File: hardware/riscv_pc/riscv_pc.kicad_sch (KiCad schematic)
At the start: 12 parts, among them J1 te_m.2_b, J2 te_m.2_b, J3 Conn_01x06, J4 HDMI_A, J5 AudioJack3, SW1 TS-1187A-C-D-B

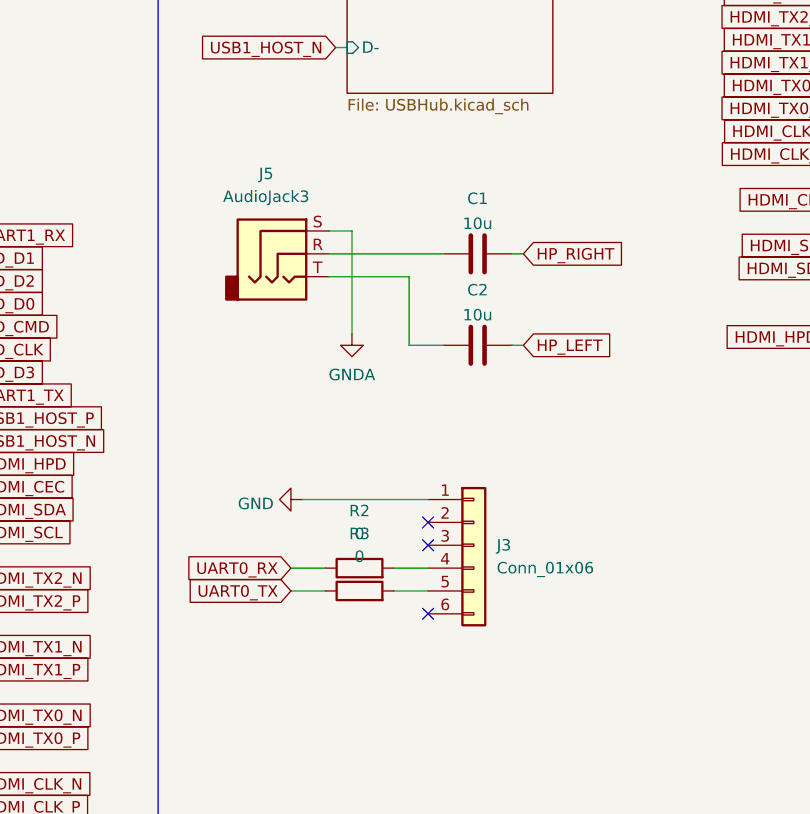
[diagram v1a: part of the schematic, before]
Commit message: Add ESD protection to AUX port
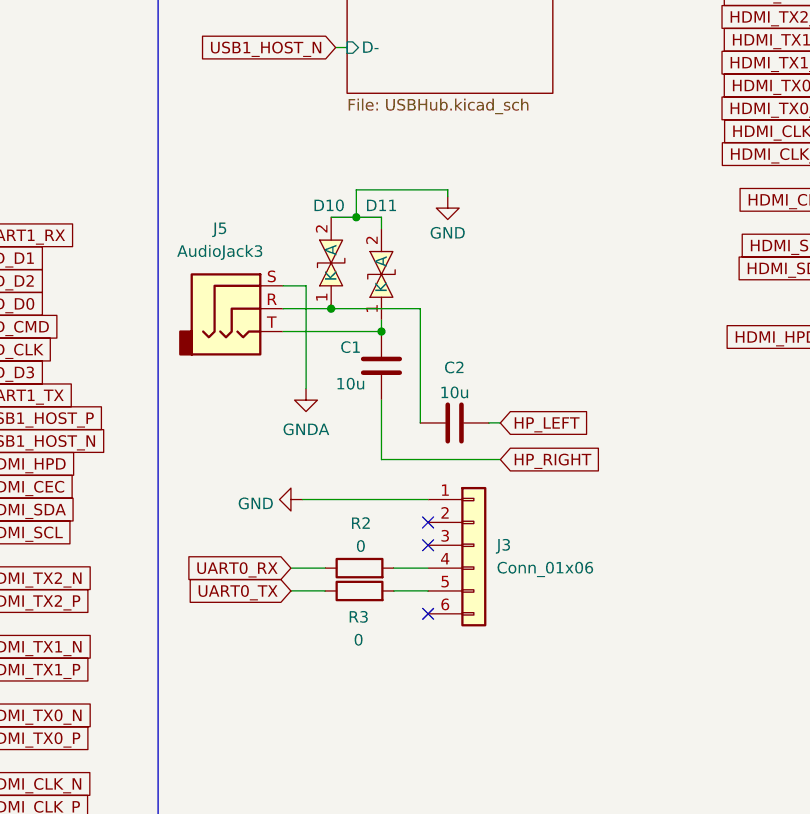
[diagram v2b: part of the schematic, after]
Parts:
- added D10, D11: GBLC08C-LF-T7, easyeda2kicad:SOD-323_L1.8-W1.3-LS2.5-BI, symbol lcsc:GBLC08C-LF-T7
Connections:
- net GND: now also D10.2 (A), D11.2 (A)
- net at C1.1: now also J5.T, D11.1 (K); no longer J5.R
- net at C2.1: now also J5.R, D10.1 (K); no longer J5.T
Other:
- moved on the sheet: C1, C2, J5

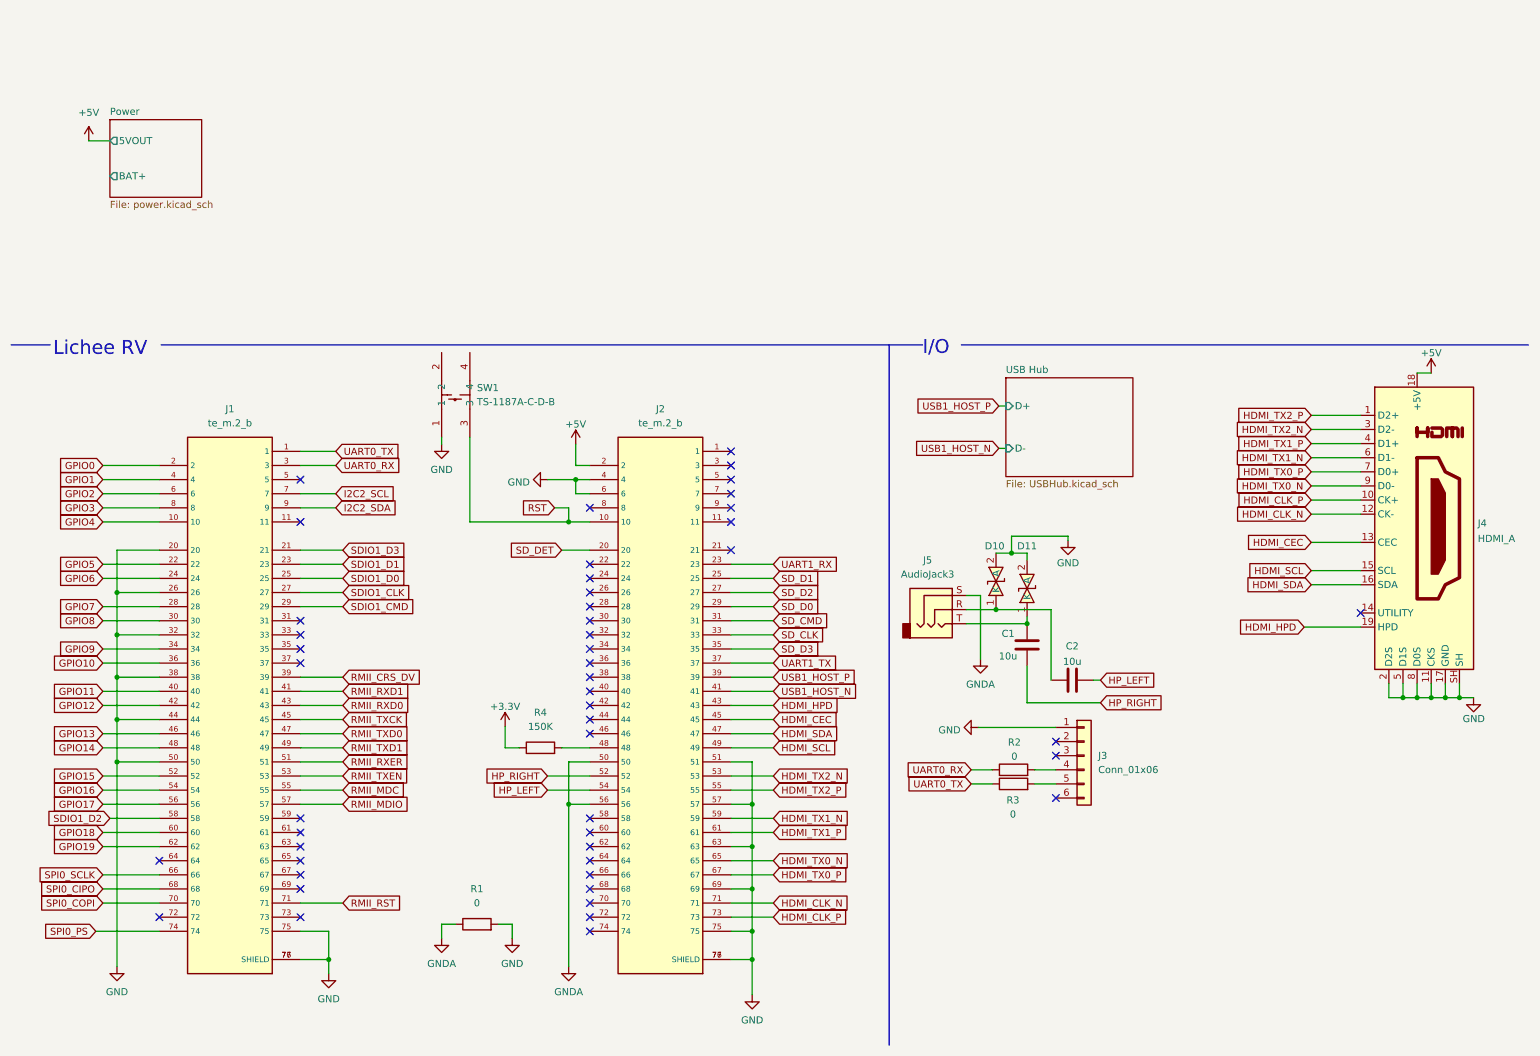
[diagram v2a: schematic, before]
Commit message: Add ESD protection to HDMI
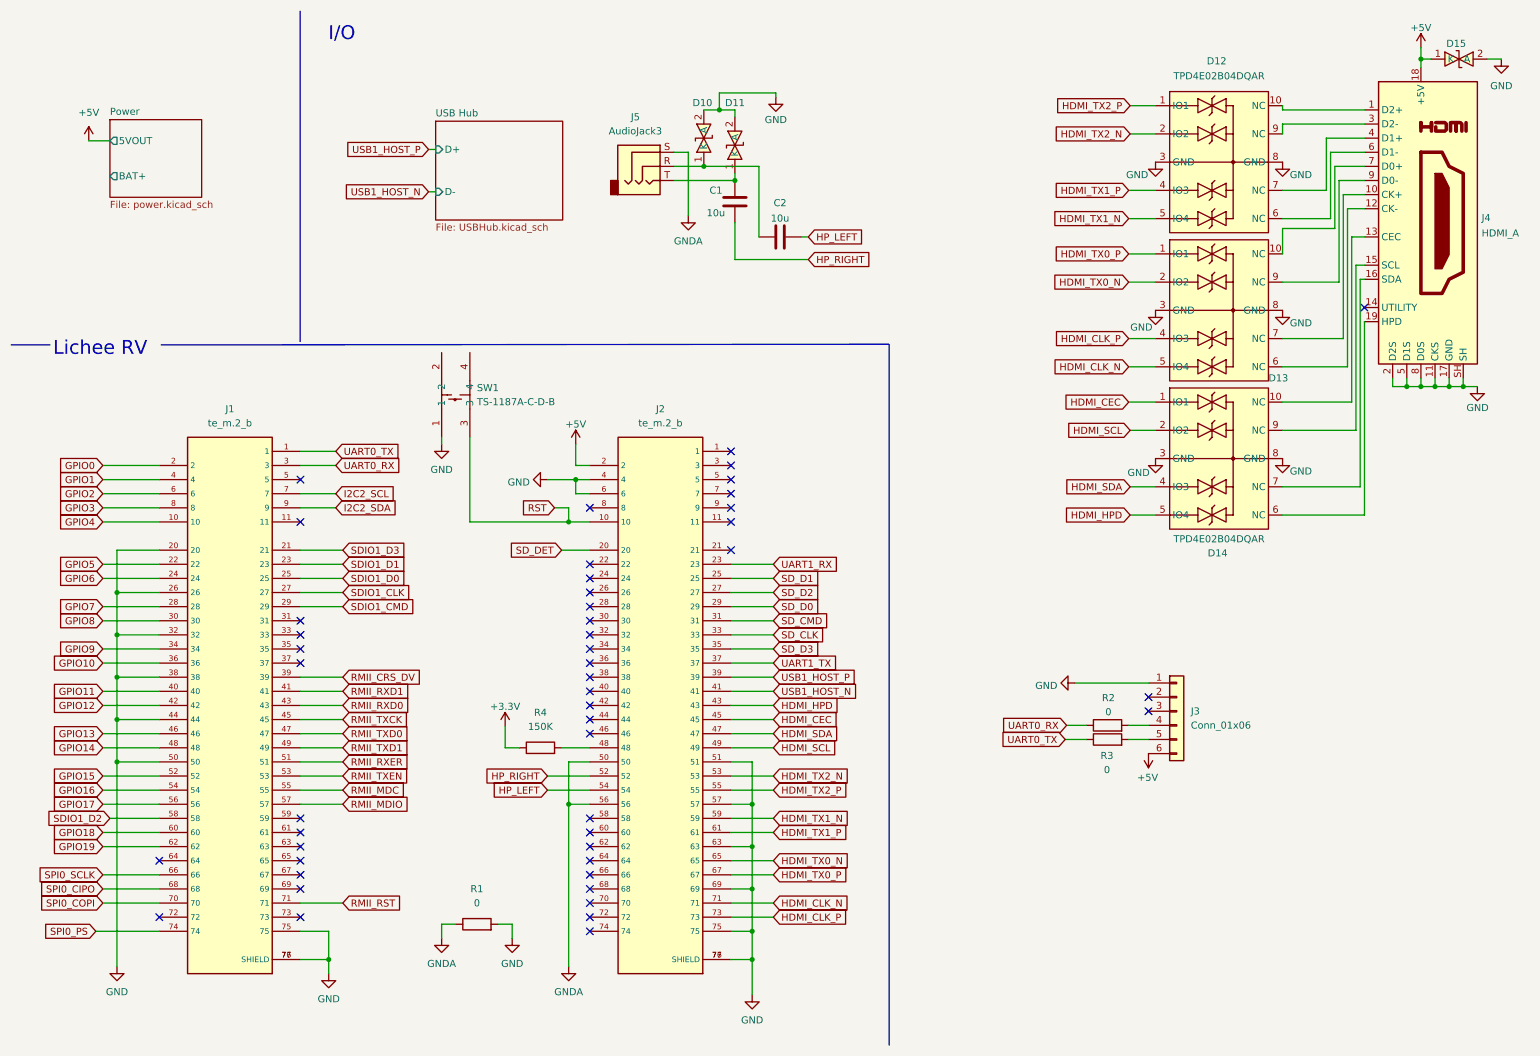
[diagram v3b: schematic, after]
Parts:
- added D12, D13, D14: TPD4E02B04DQAR, easyeda2kicad:USON-10_L2.5-W1.0-P0.50-BL, symbol lcsc:TPD4E02B04DQAR
- added D15: GBLC08C-LF-T7, easyeda2kicad:SOD-323_L1.8-W1.3-LS2.5-BI, symbol lcsc:GBLC08C-LF-T7
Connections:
- net +5V: now also J3.6 (Pin_6), D15.1 (K)
- net GND: now also D12.3 (GND), D12.8 (GND), D13.3 (GND), D13.8 (GND), D14.3 (GND), D14.8 (GND), D15.2 (A)
- net HDMI_CEC: now also D14.1 (IO1); no longer J4.13 (CEC)
- net HDMI_CLK_N: now also D13.5 (IO4); no longer J4.12 (CK-)
- net HDMI_CLK_P: now also D13.4 (IO3); no longer J4.10 (CK+)
- net HDMI_HPD: now also D14.5 (IO4); no longer J4.19 (HPD)
- net HDMI_SCL: now also D14.2 (IO2); no longer J4.15 (SCL)
- net HDMI_SDA: now also D14.4 (IO3); no longer J4.16 (SDA)
- net HDMI_TX0_N: now also D13.2 (IO2); no longer J4.9 (D0-)
- net HDMI_TX0_P: now also D13.1 (IO1); no longer J4.7 (D0+)
- net HDMI_TX1_N: now also D12.5 (IO4); no longer J4.6 (D1-)
- net HDMI_TX1_P: now also D12.4 (IO3); no longer J4.4 (D1+)
- net HDMI_TX2_N: now also D12.2 (IO2); no longer J4.3 (D2-)
- net HDMI_TX2_P: now also D12.1 (IO1); no longer J4.1 (D2+)
- new net: D13.10 (NC), J4.7 (D0+)
- new net: D13.6 (NC), J4.12 (CK-)
- new net: D13.7 (NC), J4.10 (CK+)
- new net: D13.9 (NC), J4.9 (D0-)
- new net: D12.10 (NC), J4.1 (D2+)
- new net: D14.10 (NC), J4.13 (CEC)
- new net: D14.9 (NC), J4.15 (SCL)
- new net: D14.7 (NC), J4.16 (SDA)
- new net: D14.6 (NC), J4.19 (HPD)
- new net: D12.9 (NC), J4.3 (D2-)
- new net: D12.7 (NC), J4.4 (D1+)
- new net: D12.6 (NC), J4.6 (D1-)
- no-connect marks 49 -> 48
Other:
- moved on the sheet: C1, C2, D10, D11, J3, J4, J5, R2, R3

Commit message: Add GPIO Header (2x15)
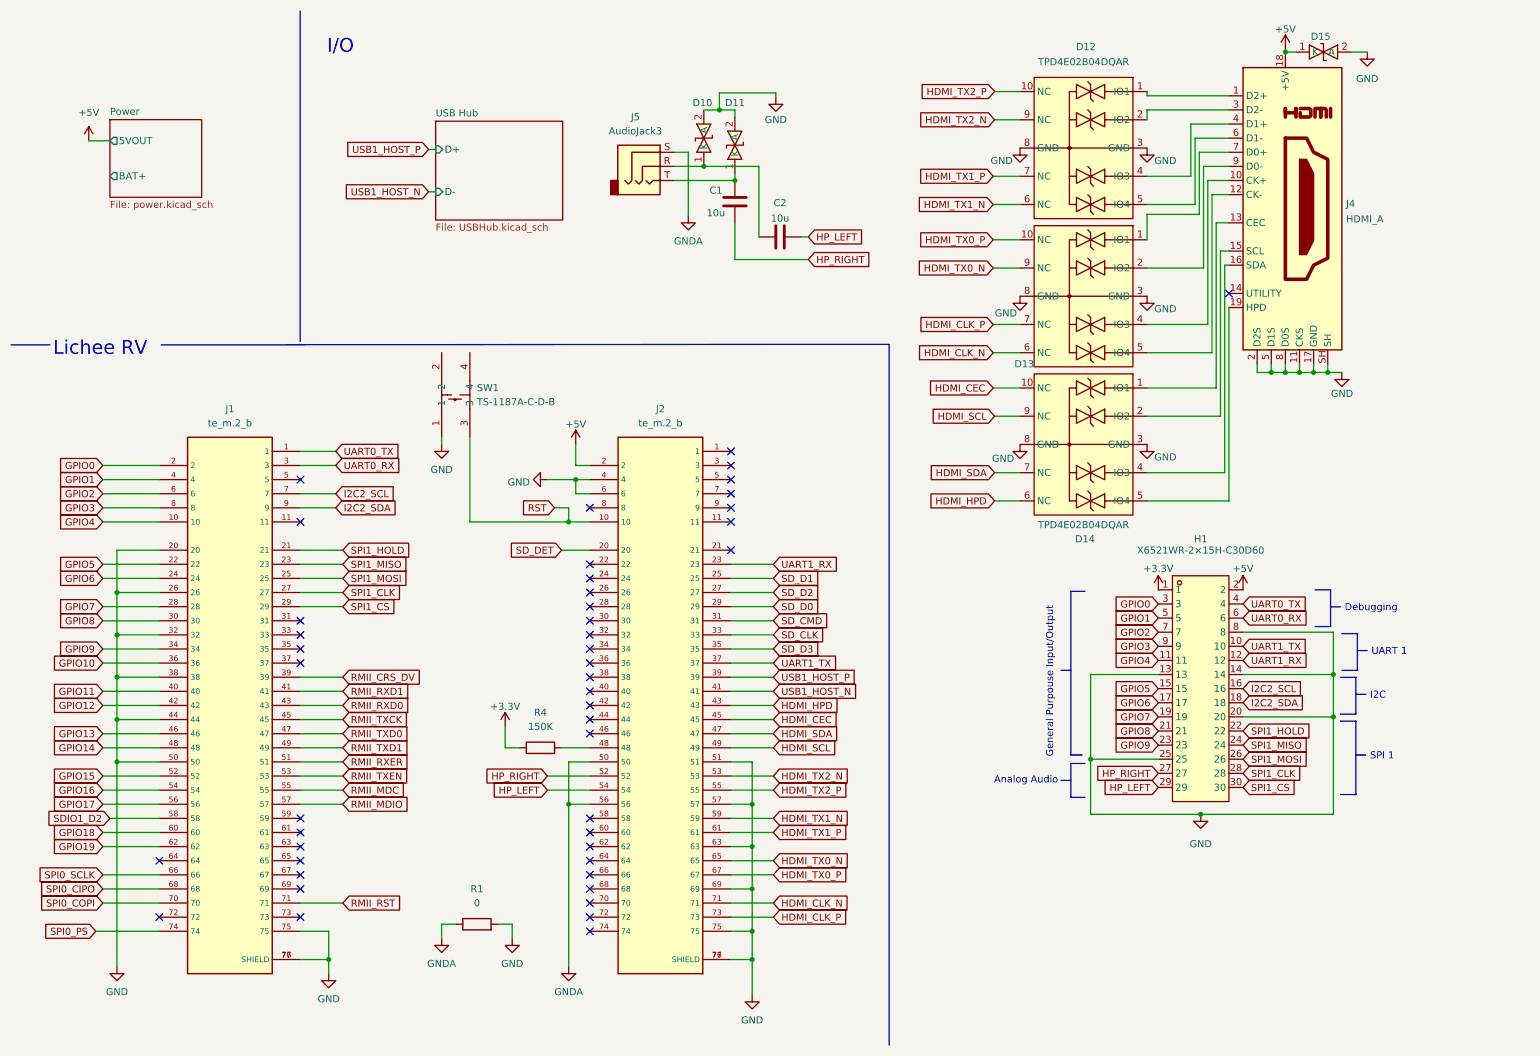
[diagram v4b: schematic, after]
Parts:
- removed J3: Conn_01x06, Connector_PinHeader_2.54mm:PinHeader_1x06_P2.54mm_Vertical, symbol Connector_Generic:Conn_01x06
- removed R2, R3: 0, Resistor_SMD:R_0603_1608Metric, symbol Device:R
- added H1: X6521WR-2×15H-C30D60, easyeda2kicad:HDR-TH_30P-P2.54-H-M-R2-C15-S2.54, symbol lcsc:X6521WR-2×15H-C30D60
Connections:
- net +5V: now also H1.2
- net GND: now also H1.13, H1.14, H1.20, H1.25, H1.8
- net GPIO0: now also H1.3
- net GPIO1: now also H1.5
- net GPIO2: now also H1.7
- net GPIO3: now also H1.9
- net GPIO4: now also H1.11
- net GPIO5: now also H1.15
- net GPIO6: now also H1.17
- net GPIO7: now also H1.19
- net GPIO8: now also H1.21
- net GPIO9: now also H1.23
- net HDMI_CEC: now also D14.10 (NC); no longer D14.1 (IO1)
- net HDMI_CLK_N: now also D13.6 (NC); no longer D13.5 (IO4)
- net HDMI_CLK_P: now also D13.7 (NC); no longer D13.4 (IO3)
- net HDMI_HPD: now also D14.6 (NC); no longer D14.5 (IO4)
- net HDMI_SCL: now also D14.9 (NC); no longer D14.2 (IO2)
- net HDMI_SDA: now also D14.7 (NC); no longer D14.4 (IO3)
- net HDMI_TX0_N: now also D13.9 (NC); no longer D13.2 (IO2)
- net HDMI_TX0_P: now also D13.10 (NC); no longer D13.1 (IO1)
- net HDMI_TX1_N: now also D12.6 (NC); no longer D12.5 (IO4)
- net HDMI_TX1_P: now also D12.7 (NC); no longer D12.4 (IO3)
- net HDMI_TX2_N: now also D12.9 (NC); no longer D12.2 (IO2)
- net HDMI_TX2_P: now also D12.10 (NC); no longer D12.1 (IO1)
- net HP_LEFT: now also H1.29
- net HP_RIGHT: now also H1.27
- net I2C2_SCL: now also H1.16
- net I2C2_SDA: now also H1.18
- net UART0_RX: now also H1.6
- net UART0_TX: now also H1.4
- net UART1_RX: now also H1.12
- net UART1_TX: now also H1.10
- net at J4.7 (D0+): now also D13.1 (IO1); no longer D13.10 (NC)
- net at J4.12 (CK-): now also D13.5 (IO4); no longer D13.6 (NC)
- net at J4.10 (CK+): now also D13.4 (IO3); no longer D13.7 (NC)
- net at J4.9 (D0-): now also D13.2 (IO2); no longer D13.9 (NC)
- net at J4.1 (D2+): now also D12.1 (IO1); no longer D12.10 (NC)
- net at J4.13 (CEC): now also D14.1 (IO1); no longer D14.10 (NC)
- net at J4.15 (SCL): now also D14.2 (IO2); no longer D14.9 (NC)
- net at J4.16 (SDA): now also D14.4 (IO3); no longer D14.7 (NC)
- net at J4.19 (HPD): now also D14.5 (IO4); no longer D14.6 (NC)
- net at J4.3 (D2-): now also D12.2 (IO2); no longer D12.9 (NC)
- net at J4.4 (D1+): now also D12.4 (IO3); no longer D12.7 (NC)
- net at J4.6 (D1-): now also D12.5 (IO4); no longer D12.6 (NC)
- net SDIO1_CLK renamed SPI1_CLK
- net SPI1_CLK: now also H1.28
- net SDIO1_CMD renamed SPI1_CS
- net SPI1_CS: now also H1.30
- net SDIO1_D0 renamed SPI1_MOSI
- net SPI1_MOSI: now also H1.26
- net SDIO1_D1 renamed SPI1_MISO
- net SPI1_MISO: now also H1.24
- net SDIO1_D3 renamed SPI1_HOLD
- net SPI1_HOLD: now also H1.22
- new net +3.3V: H1.1
- no-connect marks 48 -> 46
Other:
- note added: "Analog Audio"
- note added: "Debugging"
- note added: "General Purpouse Input/Output"
- note added: "I2C"
- note added: "SPI 1"
- note added: "UART 1"
- moved on the sheet: D12, D13, D14, D15, J4
